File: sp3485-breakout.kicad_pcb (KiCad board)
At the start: 2 copper layers, 12.7 x 10.2 mm, 5 parts, among them J1 Conn_01x04, J2 Conn_01x04, U1 SP3485CN

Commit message: Add condensor
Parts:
- added C1: 0.1u, Capacitor_SMD:C_0402_1005Metric, F.Cu at (151.1, 75.5)
- R1: footprint Resistor_SMD:R_0603_1608Metric -> Resistor_SMD:R_0402_1005Metric
- moved R1 0.91 mm to (152.4, 75.5), turned to 270 degrees
- moved U1 0.08 mm to (153.0, 80.2)
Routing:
- net VCC: track 9.71 -> 11.4 mm
- net GND: track 4.27 -> 5.10 mm, vias 1 -> 2
- net /B: track 10.2 -> 9.41 mm
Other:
- board text added: "Rev2022.01"
- board text removed: "Rev2020.11"

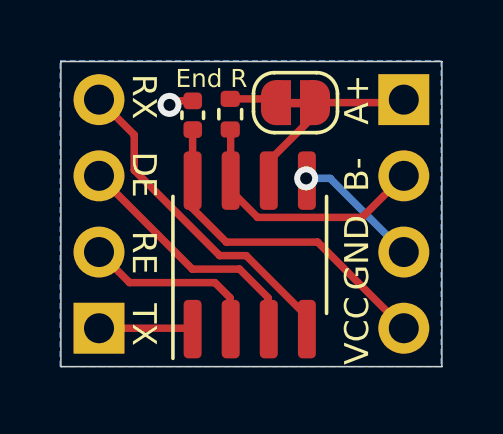
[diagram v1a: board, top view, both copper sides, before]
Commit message: Update data for KiCad8
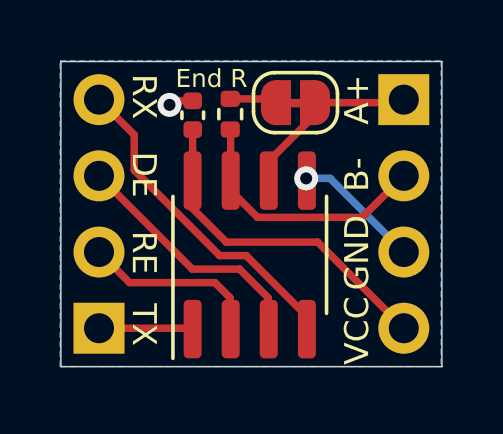
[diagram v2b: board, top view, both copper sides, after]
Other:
- net class Default removed
